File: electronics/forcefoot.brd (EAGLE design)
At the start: 55 x 45.2 mm, 62 parts

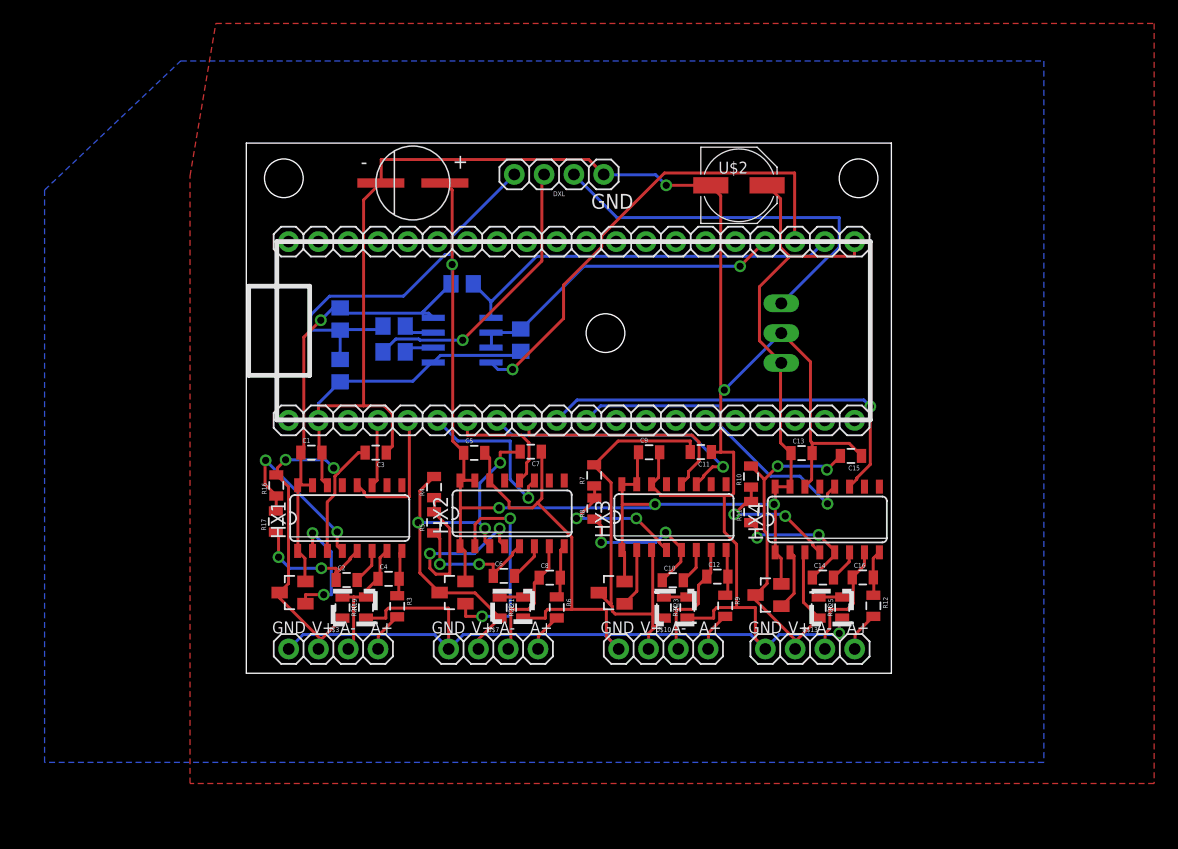
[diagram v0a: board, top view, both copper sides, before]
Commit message: Tying AGND to GND
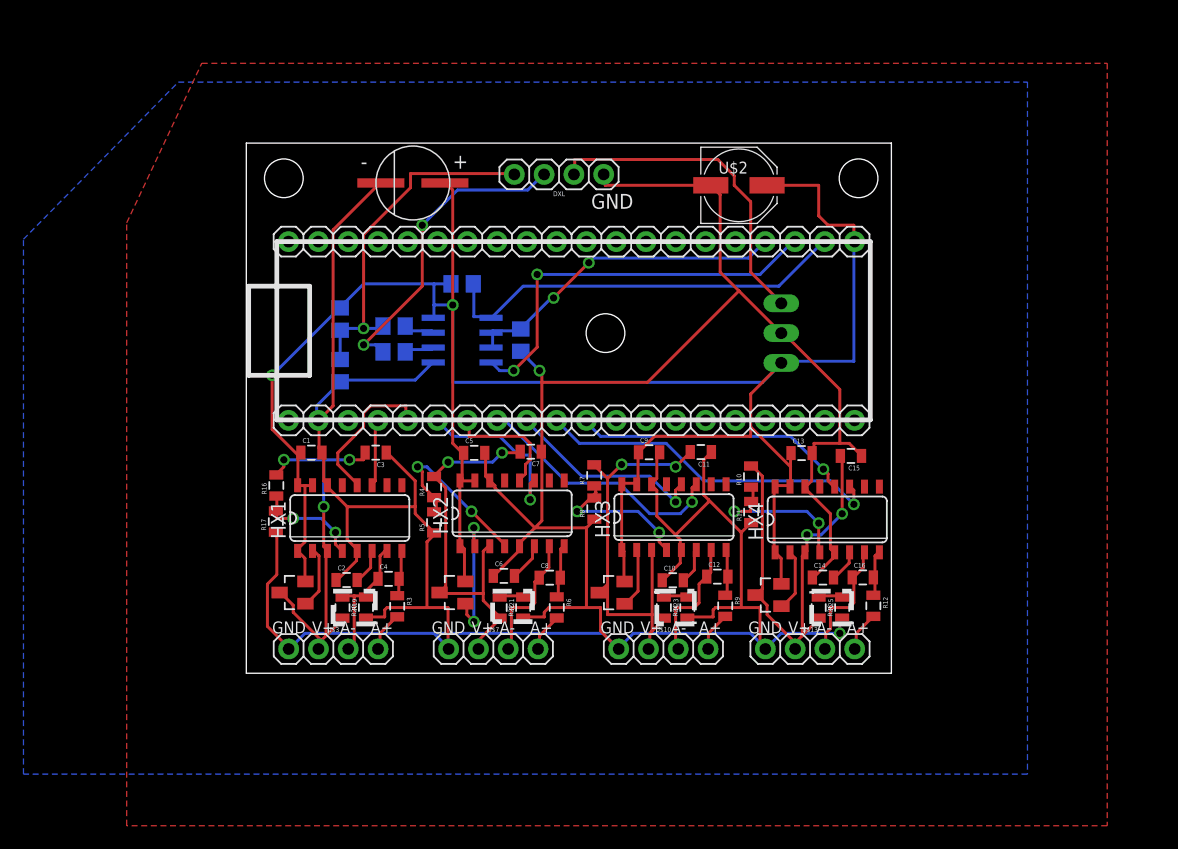
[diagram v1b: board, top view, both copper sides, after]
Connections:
- removed net AGND$1: C2.1, HX1.5, R17.1
- removed net AGND$2: C6.1, HX2.5, R5.1
- removed net AGND$3: C10.1, HX3.5, R8.1
- removed net AGND$4: C14.1, HX4.5, R11.1
- net GND: now also C10.1, C14.1, C2.1, C6.1, HX1.5, HX2.5, HX3.5, HX4.5, R11.1, R17.1, R5.1, R8.1
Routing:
- net GND: track 272.9 -> 319.9 mm, vias 3 -> 2
- net VCC: track 164.0 -> 191.6 mm, vias 5 -> 2
- net AGND$3: track 13.4 -> 0.00 mm, vias 2 -> 0
- net AGND$2: track 11.9 -> 0.00 mm, vias 2 -> 0
- net AGND$4: track 11.8 -> 0.00 mm, vias 2 -> 0
- net AGND$1: track 11.2 -> 0.00 mm, vias 2 -> 0
- net 2BASE: track 18.3 -> 11.4 mm
- net TX: track 41.2 -> 34.4 mm, vias 1 -> 2
- net VFB$1: track 15.2 -> 9.31 mm
- net VIN: track 33.6 -> 28.0 mm
- net SCK4: track 35.3 -> 30.0 mm
- net 1BASE: track 10.4 -> 5.31 mm, vias 2 -> 0
- net VFB$2: track 18.8 -> 15.0 mm
- net AVDD$2: track 36.7 -> 33.0 mm, vias 3 -> 2
- net AVDD$4: track 35.2 -> 38.7 mm
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
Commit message: Tweaking for v2
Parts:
- removed DXL: CONNEC_1X04, rhoban:CONNEC_1X04
- removed IC1: (no value), SparkFun-PowerIC:TO-220-ALT
- removed MAPLE_MINI: MAPLE_MINI, rhoban:CONNEC_2X20
- removed U$15: (no value), SparkFun-Electromechanical:STAND-OFF
- added C17, C18: 22, rhoban:C0603
- added R27: 10k, SparkFun-Passives:0805
- added R28, R29: 3K, SparkFun-Passives:0805
- added U$11, U$14: (no value), SparkFun-Electromechanical:STAND-OFF
- added U$17: GY-85, rhoban:GY-85
- added U$28: CONNEC_2X03, rhoban:CONNEC_2X03
- added U$5: REG_5V, rhoban:TRACOPOWER
- added U$8: CONNEC_1X04_485, rhoban:CONNEC_485
- added U2: ATMEGA168, SparkFun-DigitalIC:TQFP32-08
- added XTAL1: (no value), rhoban:HC49US
- U$10, U$13, U$3, U$7: value CONNEC_1X04 -> CONNEC_1X041.5; device rhoban:CONNEC_1X04 -> rhoban:4P1.5
- moved U$16 45.2 mm to (29.1, 3.11)
- moved R1 21.0 mm to (2.40, 28.2), flipped to the top
- moved C7 19.4 mm to (14.1, 2.15), turned to 90 degrees
- moved C3 18.8 mm to (1.60, 2.40), turned to 90 degrees
- moved C11 17.3 mm to (34.1, 2.05), turned to 90 degrees
- moved C15 16.3 mm to (46.9, 2.65), turned to 90 degrees
- moved R13 13.9 mm to (7.60, 24.2), flipped to the top
- moved R8 13.2 mm to (40.2, 5.87), turned to 180 degrees
- moved R11 12.9 mm to (53.7, 6.24), turned to 180 degrees
- moved R7 12.6 mm to (38.7, 7.86), turned to 180 degrees
- moved R10 12.0 mm to (51.8, 8.43), turned to 180 degrees
- moved MAX485 11.0 mm to (7.40, 28.2), flipped to the top
- moved R16 8.84 mm to (6.19, 7.76), turned to 180 degrees
- moved R5 8.49 mm to (20.7, 5.61), turned to 180 degrees
- moved R17 8.47 mm to (7.26, 5.72), turned to 180 degrees
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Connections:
- new net 3.3: R28.2, R29.2, U$17.3.3
- new net IMU_SCL: R28.1, U$17.SCL, U2.28
- new net IMU_SDA: R29.1, U$17.SDA, U2.27
- new net MISO: U$28.1, U2.16
- new net MOSI: U$28.4, U2.15
- new net N$19: C17.2, U2.7, XTAL1.2
- new net N$20: C18.2, U2.8, XTAL1.1
- new net RESET: R27.1, U$28.5, U2.29
- new net SCK: U$28.3, U2.17
- net 1A+: now also U$3.P$4; no longer U$3.4
- net 1A-: now also U$3.P$3; no longer U$3.3
- net 2A-: now also U$7.P$3; no longer U$7.3
- net 3A-: now also U$10.P$3; no longer U$10.3
- net 4A-: now also U$13.P$3; no longer U$13.3
- net AVDD$1: now also U$3.P$2; no longer U$3.2
- net AVDD$2: now also U$7.P$2; no longer U$7.2
- net AVDD$3: now also U$10.P$2; no longer U$10.2
- net AVDD$4: now also U$13.P$2; no longer U$13.2
- net DIRECTION: now also U2.32; no longer MAPLE_MINI.X2
- net DOUT1: now also U2.24; no longer MAPLE_MINI.X16
- net DOUT2: now also U2.26; no longer MAPLE_MINI.X18
- net DOUT3: now also U2.2; no longer MAPLE_MINI.X20
- net DOUT4: now also U2.22; no longer MAPLE_MINI.X22
- net GND: now also C17.1, C18.1, U$10.P$1, U$13.P$1, U$17.GND, U$28.6, U$3.P$1, U$5.P$2, U$7.P$1, U$8.GND, U2.21, U2.3, U2.5; no longer DXL.1, IC1.GND, MAPLE_MINI.GND, U$10.1, U$13.1, U$3.1, U$7.1
- net N$4: now also U$7.P$4; no longer U$7.4
- net N$6: now also U$10.P$4; no longer U$10.4
- net N$8: now also U$13.P$4; no longer U$13.4
- net RS+: now also U$8.D+; no longer DXL.3
- net RS-: now also U$8.D-; no longer DXL.4
- net RX: now also U2.30; no longer MAPLE_MINI.X0
- net SCK1: now also U2.23; no longer MAPLE_MINI.X15
- net SCK2: now also U2.25; no longer MAPLE_MINI.X17
- net SCK3: now also U2.1; no longer MAPLE_MINI.X19
- net SCK4: now also U2.19; no longer MAPLE_MINI.X21
- net TX: now also U2.31; no longer MAPLE_MINI.X1
- net VCC: now also U$17.VCC_IN, U$5.P$3; no longer IC1.OUT, MAPLE_MINI.VIN
- net VIN: now also R27.2, U$28.2, U$5.P$1, U$8.V+, U2.20, U2.4, U2.6; no longer DXL.2, IC1.IN
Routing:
- net SCK3: track 22.1 -> 69.4 mm, vias 1 -> 2
- net DOUT2: track 10.4 -> 48.8 mm
- net VIN: track 28.0 -> 65.7 mm, vias 0 -> 3
- net SCK1: track 5.71 -> 33.0 mm, vias 0 -> 2
- net RESET: track 0.00 -> 25.8 mm, vias 0 -> 2
- net DOUT1: track 13.0 -> 35.7 mm, vias 0 -> 2
- net MOSI: track 0.00 -> 22.1 mm, vias 0 -> 2
- net IMU_SCL: track 0.00 -> 21.9 mm, vias 0 -> 1
- net MISO: track 0.00 -> 21.8 mm, vias 0 -> 1
- net SCK: track 0.00 -> 21.6 mm, vias 0 -> 1
- net AVDD$4: track 38.7 -> 18.7 mm, vias 2 -> 0
- net DOUT3: track 17.3 -> 35.2 mm, vias 1 -> 2
- net AVDD$3: track 36.3 -> 18.8 mm, vias 2 -> 0
- net IMU_SDA: track 0.00 -> 16.6 mm, vias 0 -> 1
- net AVDD$2: track 33.0 -> 18.6 mm, vias 2 -> 0
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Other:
- board size 55 x 45.2 mm -> 60 x 43.6 mm
- board text removed: "A+"
- board text removed: "A-"
- board text removed: "GND"
- board text removed: "V+"

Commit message: Fixing r value
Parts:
- R14, R15: value 3k -> 22
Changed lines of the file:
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@@
 <element name="R2" library="rhoban" package="R0805" value="3k" x="6.6" y="33.2" rot="R180"/>
 <element name="R18" library="rhoban" package="R0805" value="3k" x="11" y="33.2" rot="R180"/>
-<element name="R14" library="rhoban" package="R0805" value="3k" x="13.2" y="27.2" rot="R180"/>
-<element name="R15" library="rhoban" package="R0805" value="3k" x="13.2" y="29.4" rot="R180"/>
+<element name="R14" library="rhoban" package="R0805" value="22" x="13.2" y="27.2" rot="R180"/>
+<element name="R15" library="rhoban" package="R0805" value="22" x="13.2" y="29.4" rot="R180"/>
 <element name="R19" library="SparkFun-Passives" package="0805" value="3K" x="5.8" y="3.8"/>
 <element name="R20" library="SparkFun-Passives" package="0805" value="3K" x="3.6" y="2.4" rot="R90"/>

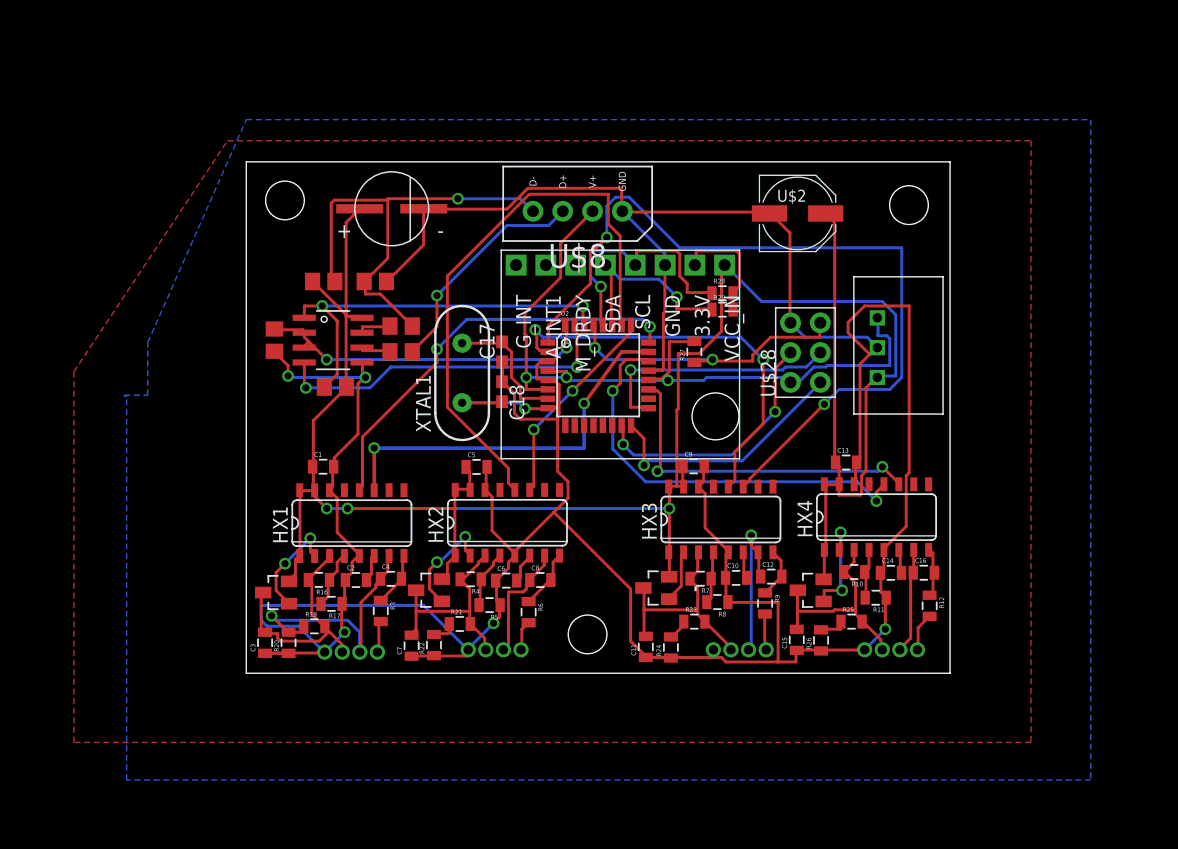
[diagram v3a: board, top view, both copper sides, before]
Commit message: Fixing vin -> vcc for mcu
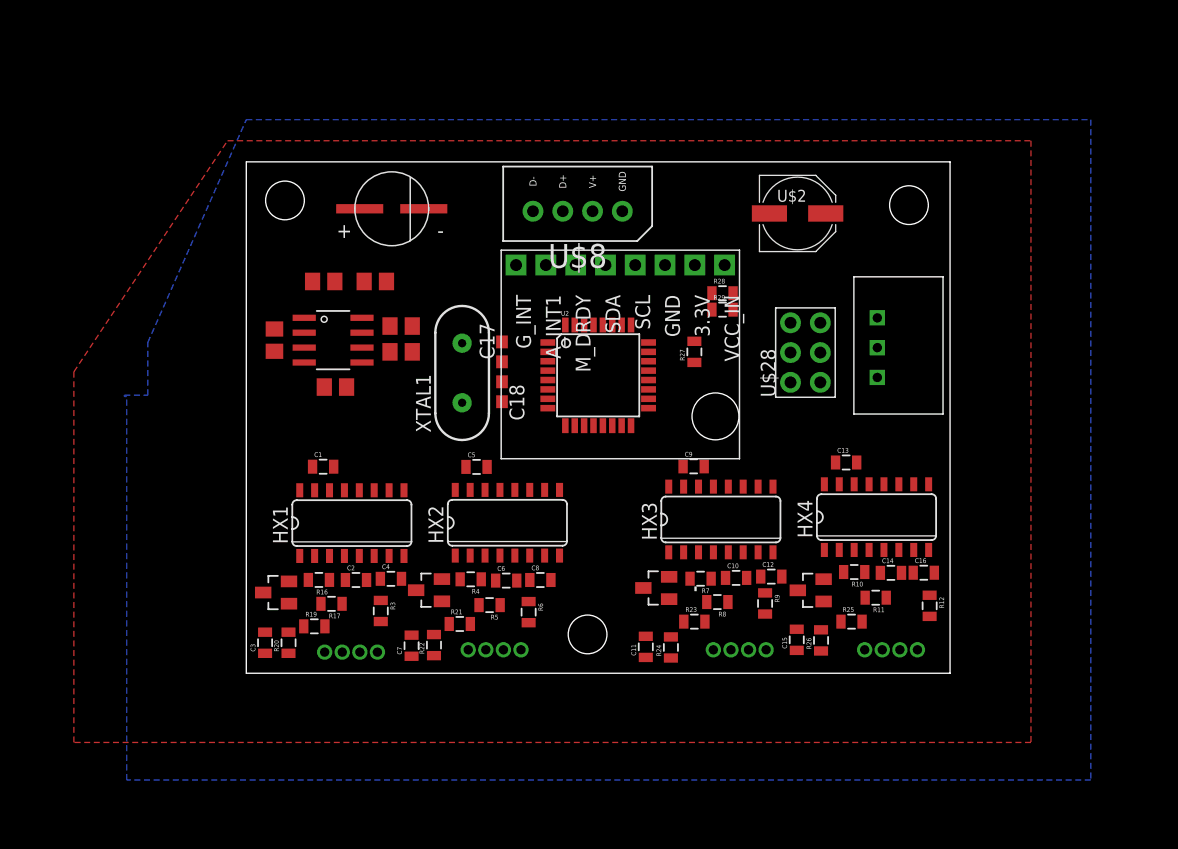
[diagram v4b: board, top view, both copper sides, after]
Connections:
- net VCC: now also U$28.2, U2.20, U2.4, U2.6
- net VIN: no longer U$28.2, U2.20, U2.4, U2.6
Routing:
- net GND: track 310.5 -> 0.00 mm, vias 5 -> 0
- net VCC: track 194.7 -> 0.00 mm, vias 3 -> 0
- net SCK3: track 69.4 -> 0.00 mm, vias 2 -> 0
- net VIN: track 65.7 -> 0.00 mm, vias 3 -> 0
- net DOUT2: track 48.8 -> 0.00 mm
- net RS-: track 38.7 -> 0.00 mm, vias 1 -> 0
- net DOUT4: track 36.2 -> 0.00 mm, vias 2 -> 0
- net DOUT1: track 35.7 -> 0.00 mm, vias 2 -> 0
- net DOUT3: track 35.2 -> 0.00 mm, vias 2 -> 0
- net RX: track 34.3 -> 0.00 mm, vias 2 -> 0
- net SCK1: track 33.0 -> 0.00 mm, vias 2 -> 0
- net TX: track 29.8 -> 0.00 mm, vias 2 -> 0
- net DIRECTION: track 29.4 -> 0.00 mm, vias 2 -> 0
- net SCK4: track 29.3 -> 0.00 mm, vias 2 -> 0
- net RESET: track 25.8 -> 0.00 mm, vias 2 -> 0
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
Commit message: Fixes
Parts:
- moved U$28 14.0 mm to (47.2, 38.6), turned to 180 degrees
- moved U$2 11.4 mm to (46.8, 27.6), turned to 90 degrees
- moved U2 0.36 mm to (30.2, 25.5)
- moved R9 0.30 mm to (44.2, 5.45)
- moved R19 0.14 mm to (5.90, 3.90)
- moved R22 0.10 mm to (16.0, 2.10)
- moved C11 0.10 mm to (34.2, 2.05)
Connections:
- net VCC: now also R27.2
- net VIN: no longer R27.2
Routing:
- net GND: track 0.00 -> 280.4 mm, vias 0 -> 7
- net VCC: track 0.00 -> 183.1 mm, vias 0 -> 3
- net DOUT1: track 0.00 -> 55.7 mm, vias 0 -> 2
- net MISO: track 0.00 -> 53.7 mm, vias 0 -> 1
- net RX: track 0.00 -> 49.8 mm
- net RESET: track 0.00 -> 41.1 mm
- net DOUT2: track 0.00 -> 38.7 mm, vias 0 -> 2
- net SCK: track 0.00 -> 38.0 mm, vias 0 -> 2
- net SCK3: track 0.00 -> 36.5 mm, vias 0 -> 2
- net SCK1: track 0.00 -> 35.7 mm, vias 0 -> 2
- net TX: track 0.00 -> 34.1 mm, vias 0 -> 2
- net MOSI: track 0.00 -> 33.9 mm, vias 0 -> 2
- net DOUT4: track 0.00 -> 30.4 mm, vias 0 -> 2
- net DIRECTION: track 0.00 -> 30.2 mm, vias 0 -> 2
- net SCK4: track 0.00 -> 28.9 mm, vias 0 -> 2
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
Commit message: Fixing connections
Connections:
- removed net 1A-1: R21.1, R22.2
- removed net 1A-2: R23.1, R24.2
- removed net 1A-3: R25.1, R26.2
- net 2A-: now also R21.1, R22.2
- net 3A-: now also R23.1, R24.2
- net 4A-: now also R25.1, R26.2
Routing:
- net 3A-: track 8.92 -> 19.5 mm
- net 4A-: track 9.05 -> 19.2 mm
- net 2A-: track 10.2 -> 19.6 mm
- net GND: track 280.4 -> 271.0 mm, vias 7 -> 11
- net SCK4: track 28.9 -> 32.5 mm
- net VCC: track 183.1 -> 180.1 mm
- net DOUT4: track 30.4 -> 27.6 mm
- net 2BASE: track 11.5 -> 9.00 mm
- net 1A-3: track 2.40 -> 0.00 mm
- net SCK: track 38.0 -> 35.6 mm
- net 1A-1: track 2.30 -> 0.00 mm
- net MISO: track 53.7 -> 51.9 mm
- net 1A-2: track 1.76 -> 0.00 mm
- net MOSI: track 33.9 -> 35.7 mm
- net DOUT3: track 26.9 -> 27.4 mm
